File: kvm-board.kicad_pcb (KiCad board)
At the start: 2 copper layers, 65.4 x 31.4 mm, 23 parts, among them J1 TYPE-C-31-M-12, J2 TYPE-C-31-M-12, U1 CH9329, U2 CH340N

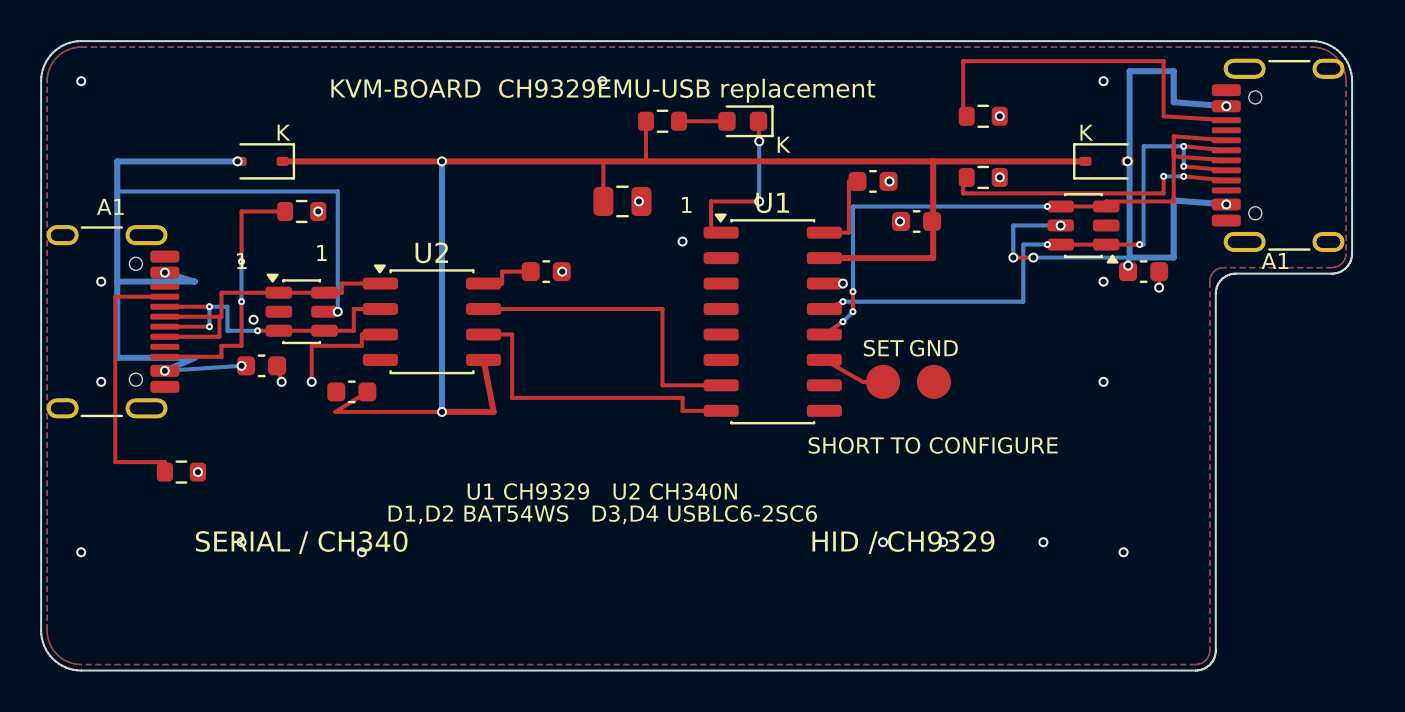
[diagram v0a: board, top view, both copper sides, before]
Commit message: Fit the board to the measured FRISK case
Widen the board to 66.0 x 31.4 mm for the 67.0 x 32.4 mm inner tray, cut an 8.4 x 20.4 mm latch notch with a square inner corner, and centre J1 at 15.7 mm so its terminal row is on the board centreline. Keep both connector mouths at the case surface (J1 1.5 mm, J2 1.44 mm overhang; 1.0 mm wall plus 0.5 mm gap). Move R1 down 0.3 mm to clear J1's courtyard and adjust the J1 escapes. Make the A4 fit sheet a solid grey board with a light grey 0.5 mm clearance band instead of outlines. Regenerate the PCB, fabrication files, images and schematic. DRC and ERC are clean.
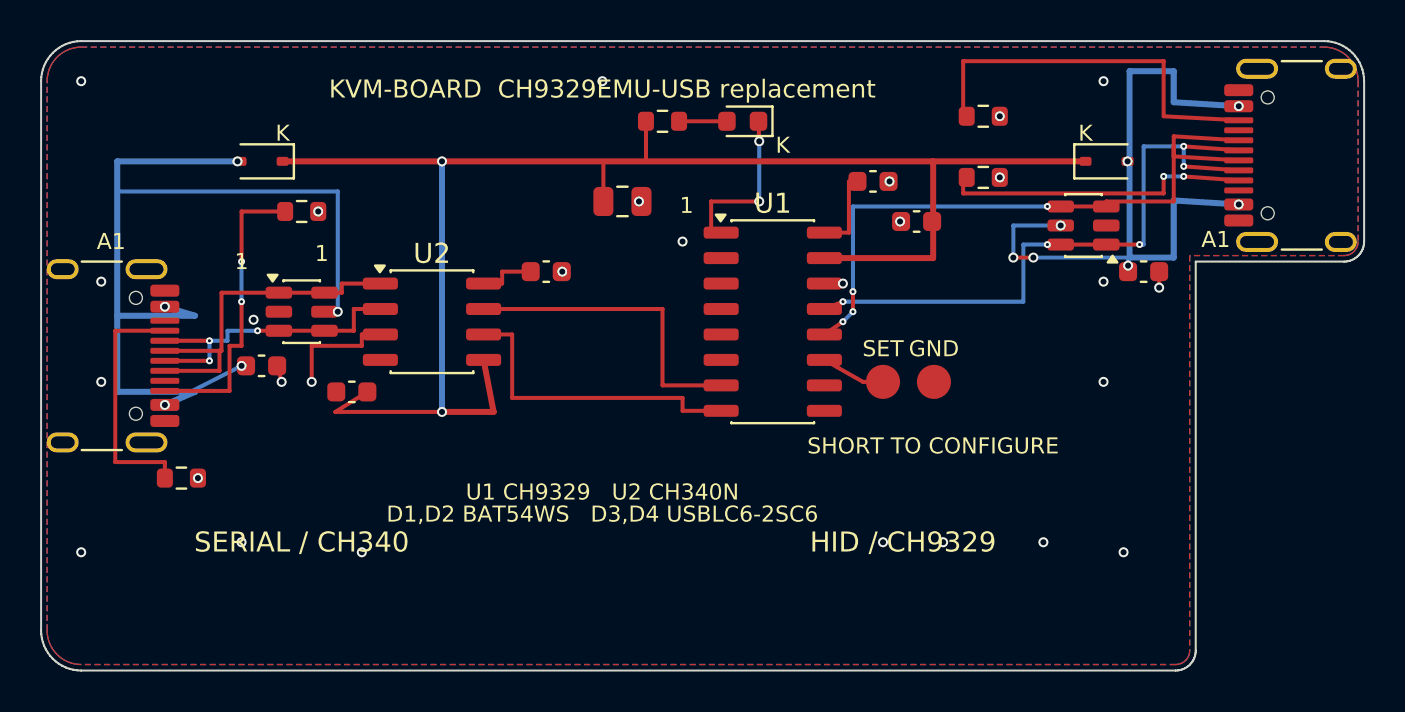
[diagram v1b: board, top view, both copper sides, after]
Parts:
- moved J1 1.70 mm to (2.13, 15.7)
- moved J2 0.62 mm to (63.8, 5.70)
- moved R1 0.30 mm to (7.00, 21.8)
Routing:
- net VBUS_SER: track 48.6 -> 50.8 mm
- net USB_SER_DP: track 16.1 -> 17.8 mm
- net CC2_SER: track 13.3 -> 15.0 mm
- net CC1_SER: track 13.7 -> 12.3 mm
- net USB_HID_DP: track 32.3 -> 33.6 mm
- net VBUS_HID: track 33.9 -> 35.1 mm
- net USB_HID_DM: track 31.0 -> 32.2 mm
- net USB_SER_DM: track 16.3 -> 15.6 mm
- net CC2_HID: track 18.8 -> 19.4 mm
- net CC1_HID: track 15.0 -> 15.6 mm
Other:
- board size 65.4 x 31.4 mm -> 66 x 31.4 mm

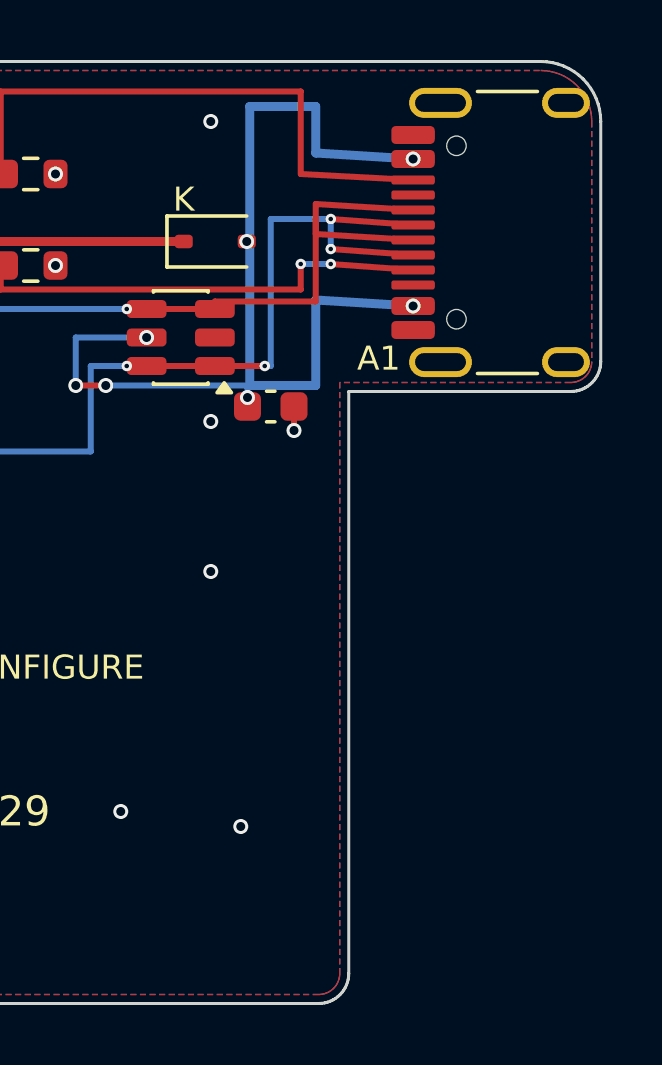
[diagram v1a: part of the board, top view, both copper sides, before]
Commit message: Leave clearance in the latch opening
Reduce the upper-right lobe from 11.0 to 10.5 mm (notch 8.4 x 20.9 mm) so the board is 0.5 mm smaller than the measured 11.0 mm opening. Nudge J2 0.16 mm left and 0.22 mm up to keep its shell pads 0.2 mm from the notch edge and the rounded corner; the J2 mouth overhang becomes 1.28 mm. Regenerate the PCB, fabrication files, images and print sheet. DRC and ERC are clean.
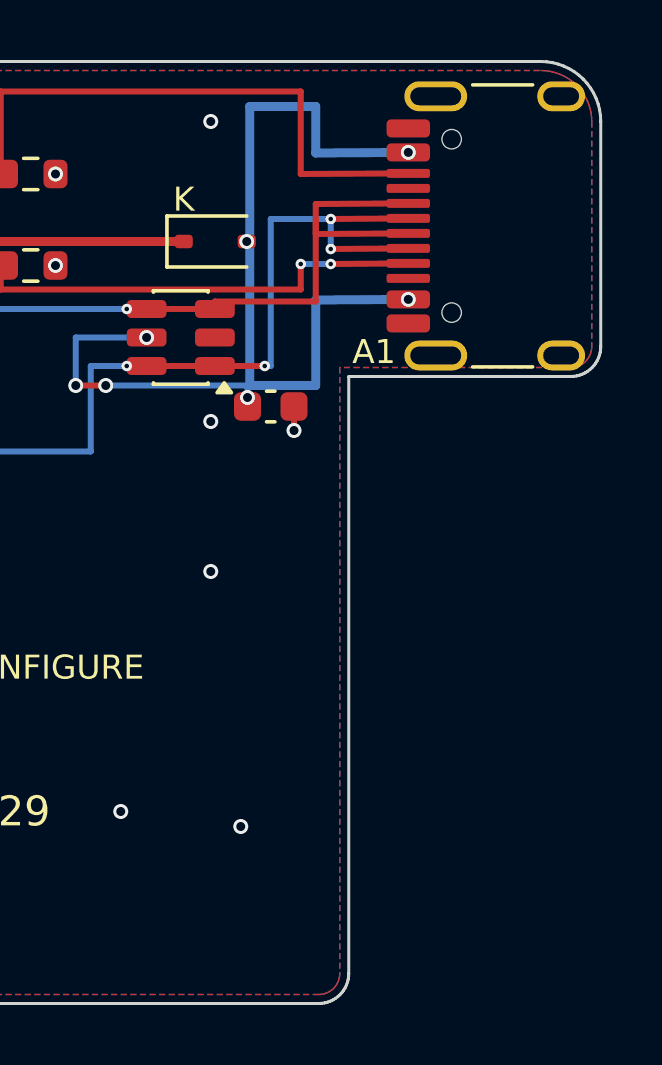
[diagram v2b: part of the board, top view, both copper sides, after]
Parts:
- moved J2 0.27 mm to (63.6, 5.48)
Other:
- outline, holes or cut-outs redrawn

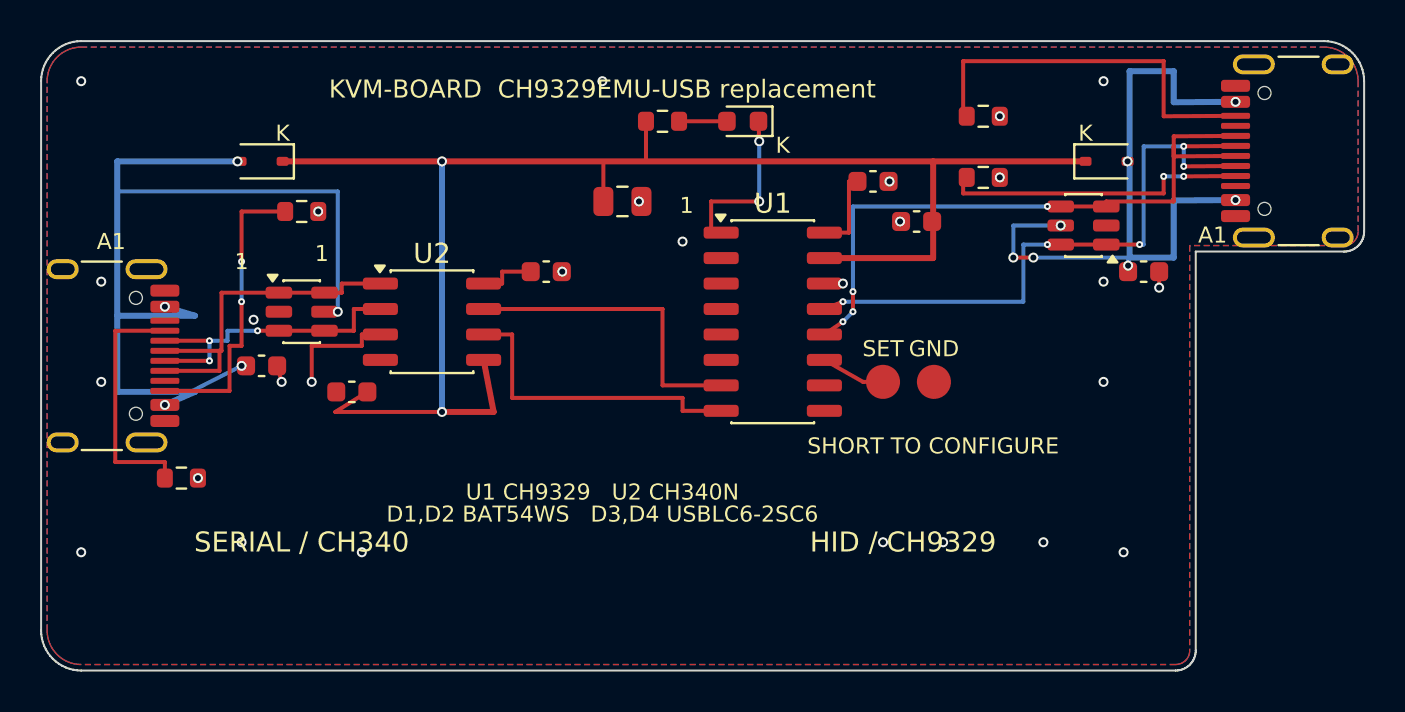
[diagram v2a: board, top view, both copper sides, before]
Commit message: Simplify the outline and put both Type-C ports on the left
Cut the whole right side back to the old latch-notch line, so the board is
57.6 x 31.4 mm with one straight right edge and no lobe.  Move J2 next to J1
on the left edge, 12.0 mm apart around the centre line, and reroute the HID
side, VBUS, CC and SET test pad around the new placement.  Regenerate the
PCB, fabrication files, images and the 1:1 fit sheet, and update the notes.
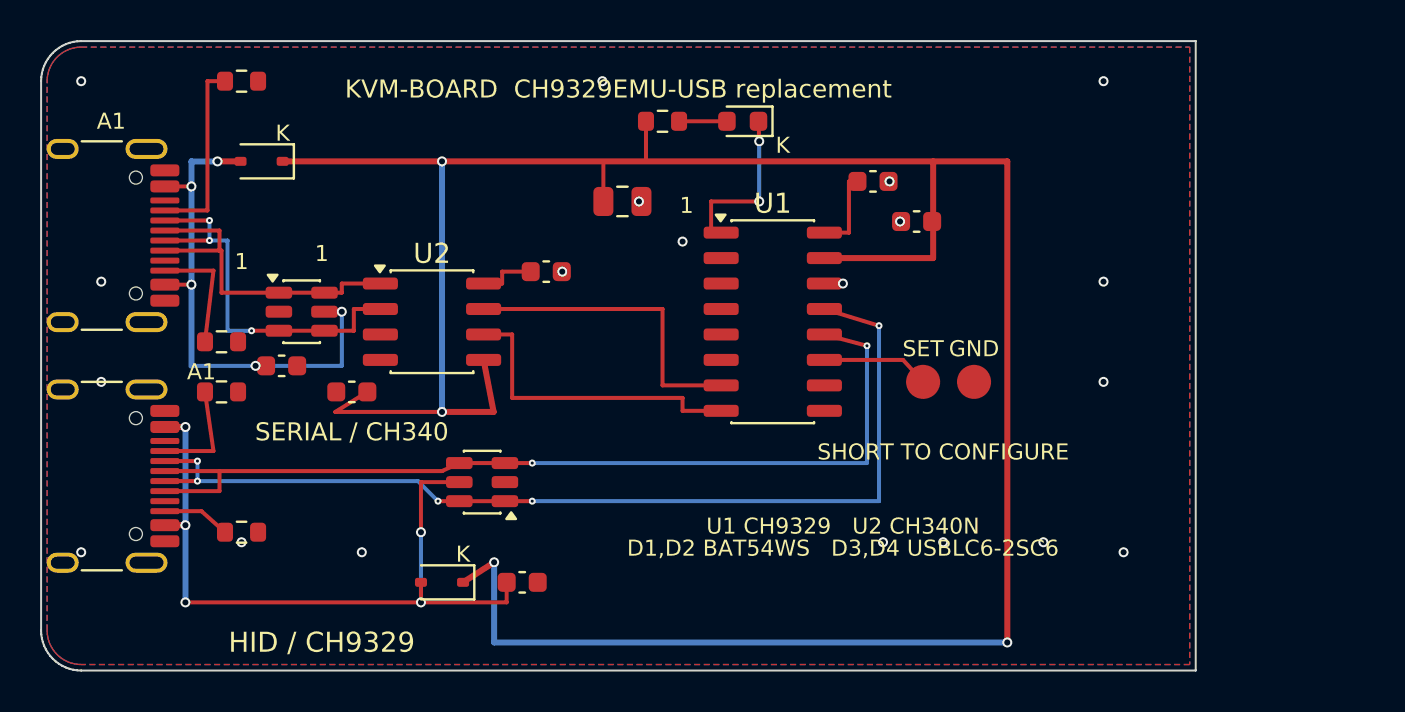
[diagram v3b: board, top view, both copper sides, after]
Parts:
- moved J2 63.6 mm to (2.13, 21.7), turned to -90 degrees
- moved R4 42.4 mm to (10.0, 24.5)
- moved R3 39.5 mm to (9.00, 17.5)
- moved D2 39.2 mm to (20.0, 27.0), turned to 180 degrees
- moved C7 34.7 mm to (24.0, 27.0)
- moved D4 32.6 mm to (22.0, 22.0)
- moved R1 20.0 mm to (10.0, 2.00)
- moved R2 7.63 mm to (9.00, 15.0)
- moved J1 6.00 mm to (2.13, 9.70)
- moved TP1 2.00 mm to (44.0, 17.0)
- moved TP2 2.00 mm to (46.5, 17.0)
- moved C6 1.00 mm to (12.0, 16.2)
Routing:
- net +5V: track 79.3 -> 130.8 mm, vias 2 -> 4
- net VBUS_SER: track 50.8 -> 26.9 mm
- net USB_HID_DM: track 31.9 -> 50.3 mm
- net CC2_HID: track 19.3 -> 3.40 mm
- net USB_HID_DP: track 33.2 -> 46.9 mm, vias 4 -> 2
- net CC1_HID: track 15.4 -> 5.41 mm, vias 2 -> 0
- net CC2_SER: track 15.0 -> 6.00 mm, vias 2 -> 0
- net GND: track 8.35 -> 0.92 mm, vias 28 -> 20
- net USB_SER_DM: track 15.6 -> 19.6 mm
- net CC1_SER: track 12.3 -> 9.45 mm
- net SET: track 3.21 -> 5.41 mm
- net VBUS_HID: track 34.8 -> 36.7 mm, vias 7 -> 5
- net USB_SER_DP: track 17.8 -> 17.0 mm
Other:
- board size 66 x 31.4 mm -> 57.6 x 31.4 mm

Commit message: Make the routing orthogonal and update the schematic size note
Replace the remaining diagonal copper segments with horizontal and vertical
runs, including the HID data pairs, CC legs, D2 supply leg, U2 VCC, SET and
the LED via jog.  Update the schematic title block to 57.6 x 31.4 mm and
regenerate the schematic, fab files and board images.
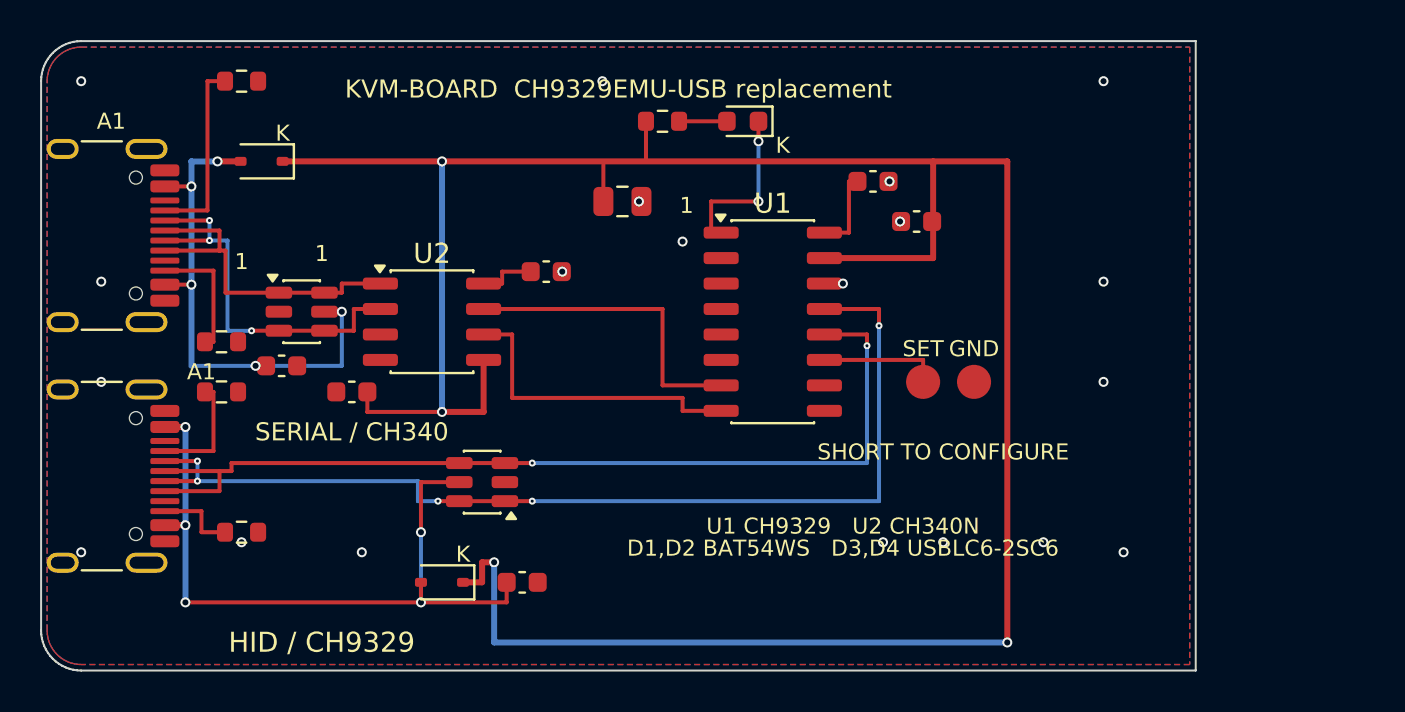
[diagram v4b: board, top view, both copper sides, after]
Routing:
- net +5V: track 130.8 -> 128.4 mm
- net USB_HID_DM: track 50.3 -> 51.6 mm
- net USB_HID_DP: track 46.9 -> 47.7 mm
- net CC2_HID: track 3.40 -> 4.05 mm
- net SET: track 5.41 -> 6.02 mm

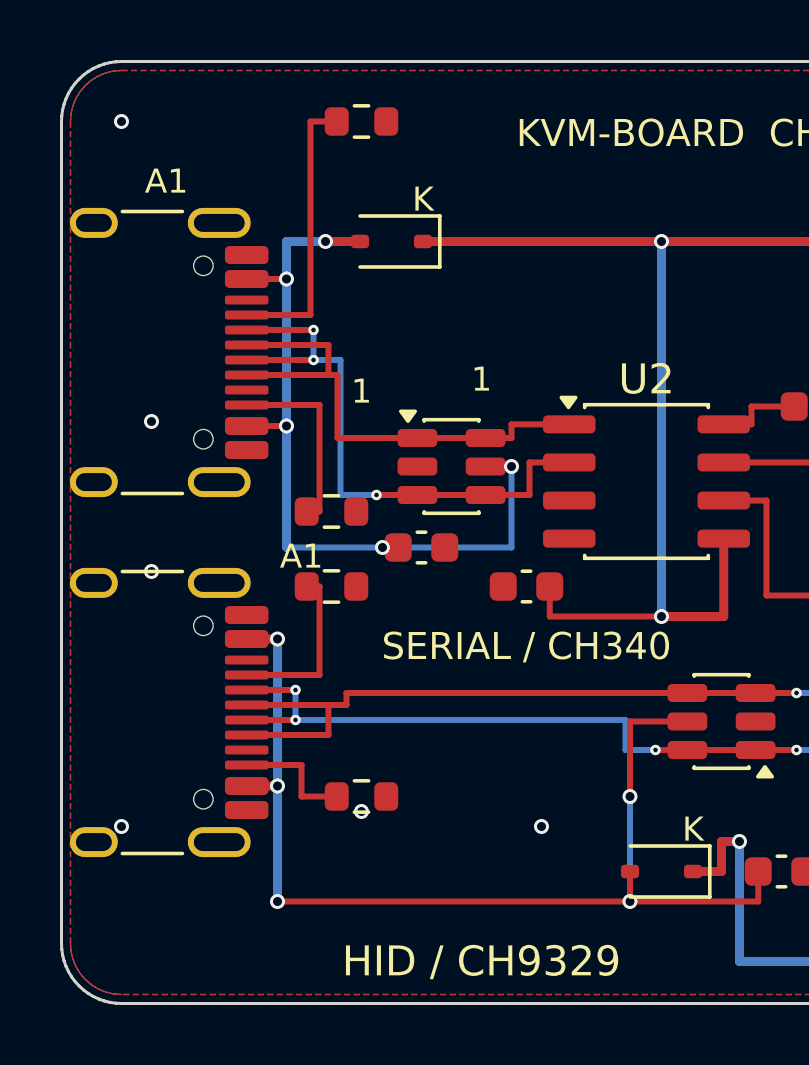
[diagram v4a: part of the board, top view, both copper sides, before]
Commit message: Move the Type-C ports inward to fit the lid notch
J1/J2 move from +/-6.0 mm to +/-5.0 mm around the board centre (pitch 12.0 -> 10.0 mm), so both mouths sit inside the FRISK lid notch and only the tray wall needs an opening. The shells keep 1.06 mm between them. Re-route the J1/J2 VBUS, D+/D- and CC escapes orthogonally, add a J1/J2-only courtyard DRC rule, and regenerate the fab files, images and print sheet.
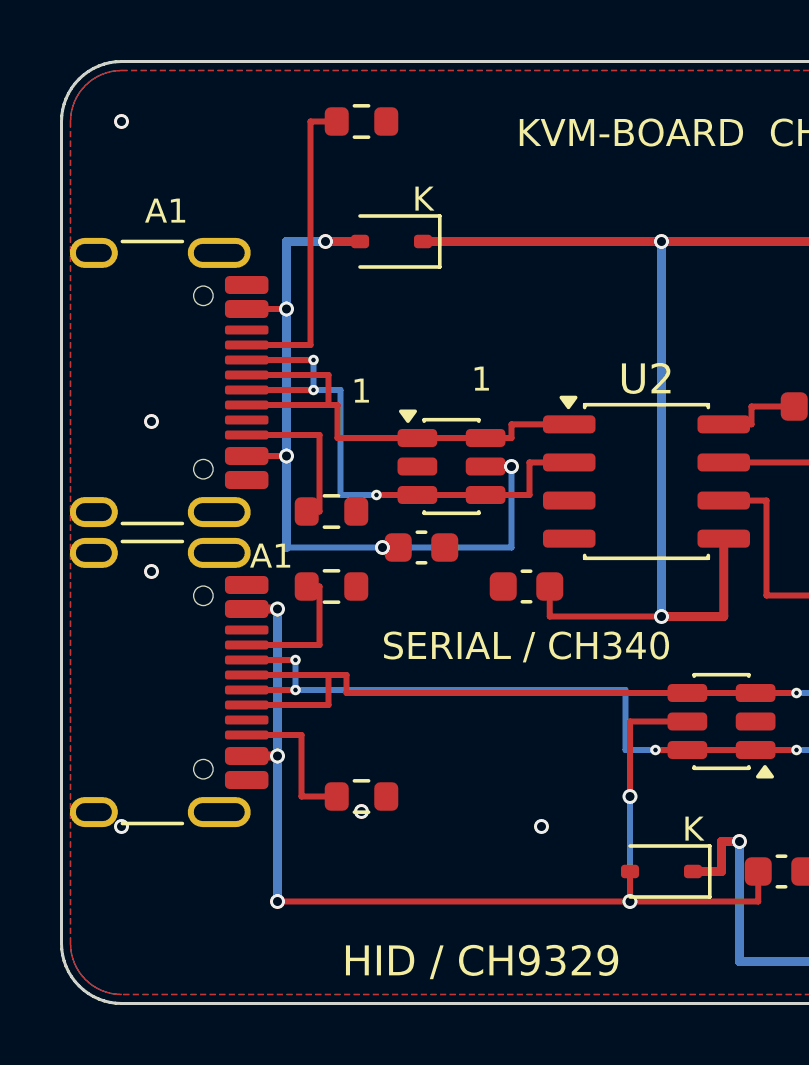
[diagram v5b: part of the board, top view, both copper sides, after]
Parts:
- moved J1 1.00 mm to (2.13, 10.7)
- moved J2 1.00 mm to (2.13, 20.7)
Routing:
- net VBUS_HID: track 36.7 -> 37.7 mm
- net USB_SER_DP: track 17.0 -> 16.0 mm
- net USB_SER_DM: track 19.6 -> 18.6 mm
- net USB_HID_DM: track 51.6 -> 52.6 mm
- net CC2_SER: track 6.40 -> 5.40 mm
- net CC2_HID: track 4.05 -> 5.05 mm
- net CC1_SER: track 9.45 -> 10.5 mm
- net CC1_HID: track 5.80 -> 4.80 mm
